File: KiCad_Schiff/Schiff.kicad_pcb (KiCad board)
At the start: 2 copper layers, 150 x 60 mm, 40 parts, among them J1 Conn_01x02, J2 L298N, J3 AMS1117-Module, J4 L298N, J5 Screw_Terminal_01x02, J6 Screw_Terminal_01x02, M1 Motor_Servo, M2 Motor_Servo, M3 Motor_Servo, SW1 SW_Wuerth_450301014042, SW2 SW_Wuerth_450301014042, U1 NRF24L01_Breakout

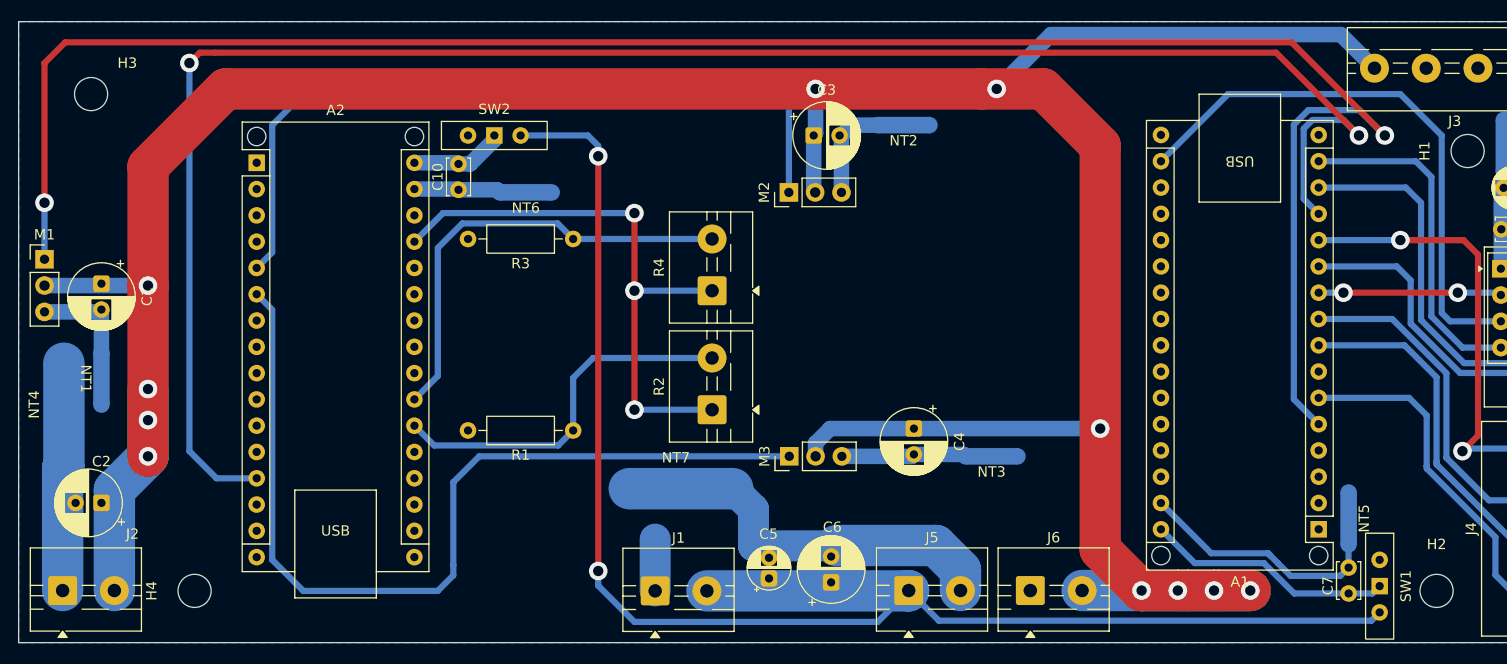
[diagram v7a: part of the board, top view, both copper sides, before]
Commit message: small changes to the PCB
New bridge on ground-plane and moved some traces for better and bigger connections on the ground-plane
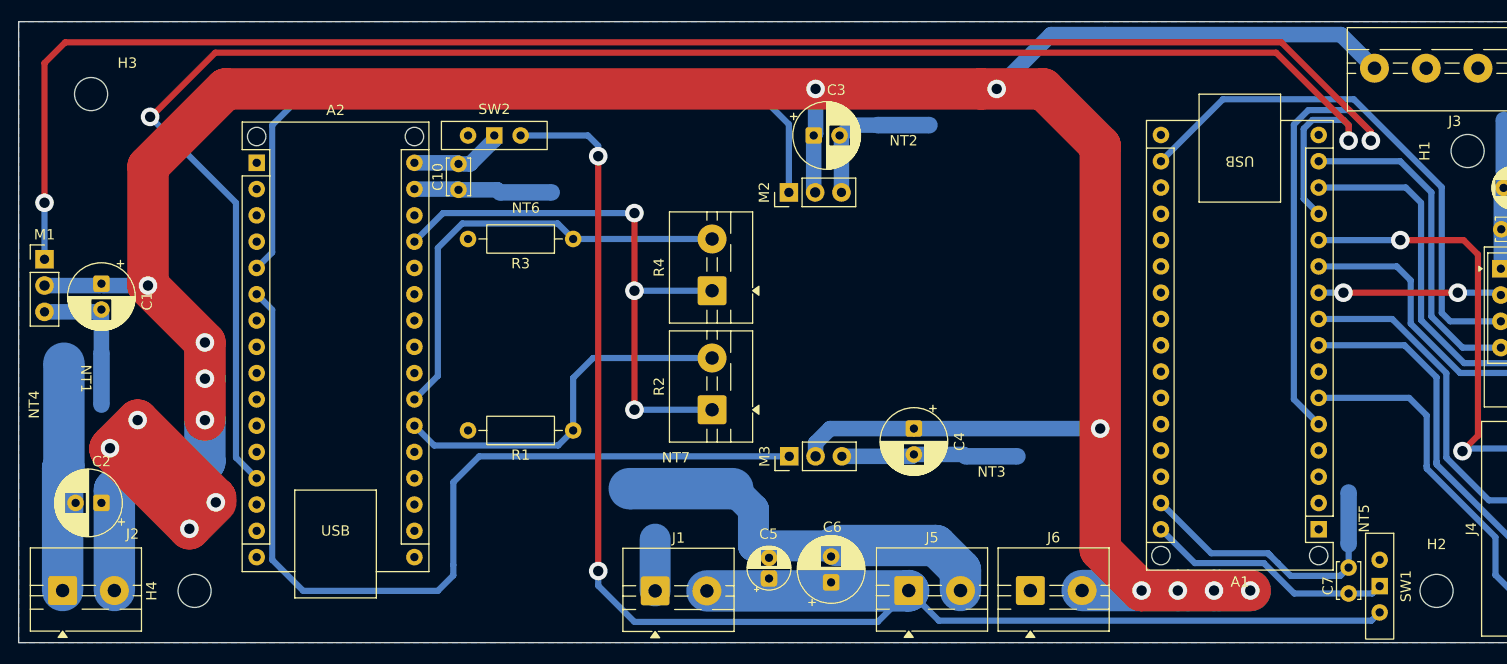
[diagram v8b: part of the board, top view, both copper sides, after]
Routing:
- net /GND_PLANE: track 5.00 -> 34.1 mm, vias 0 -> 4
- net +5V: track 307.3 -> 316.3 mm
- net /ServoFoilL: track 76.4 -> 73.0 mm
- net Net-(A1-D13): track 54.7 -> 51.3 mm
- net /ServoStear: track 193.3 -> 192.0 mm
- net Net-(A1-D12): track 33.4 -> 32.5 mm
